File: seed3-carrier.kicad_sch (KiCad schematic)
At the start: 1 part

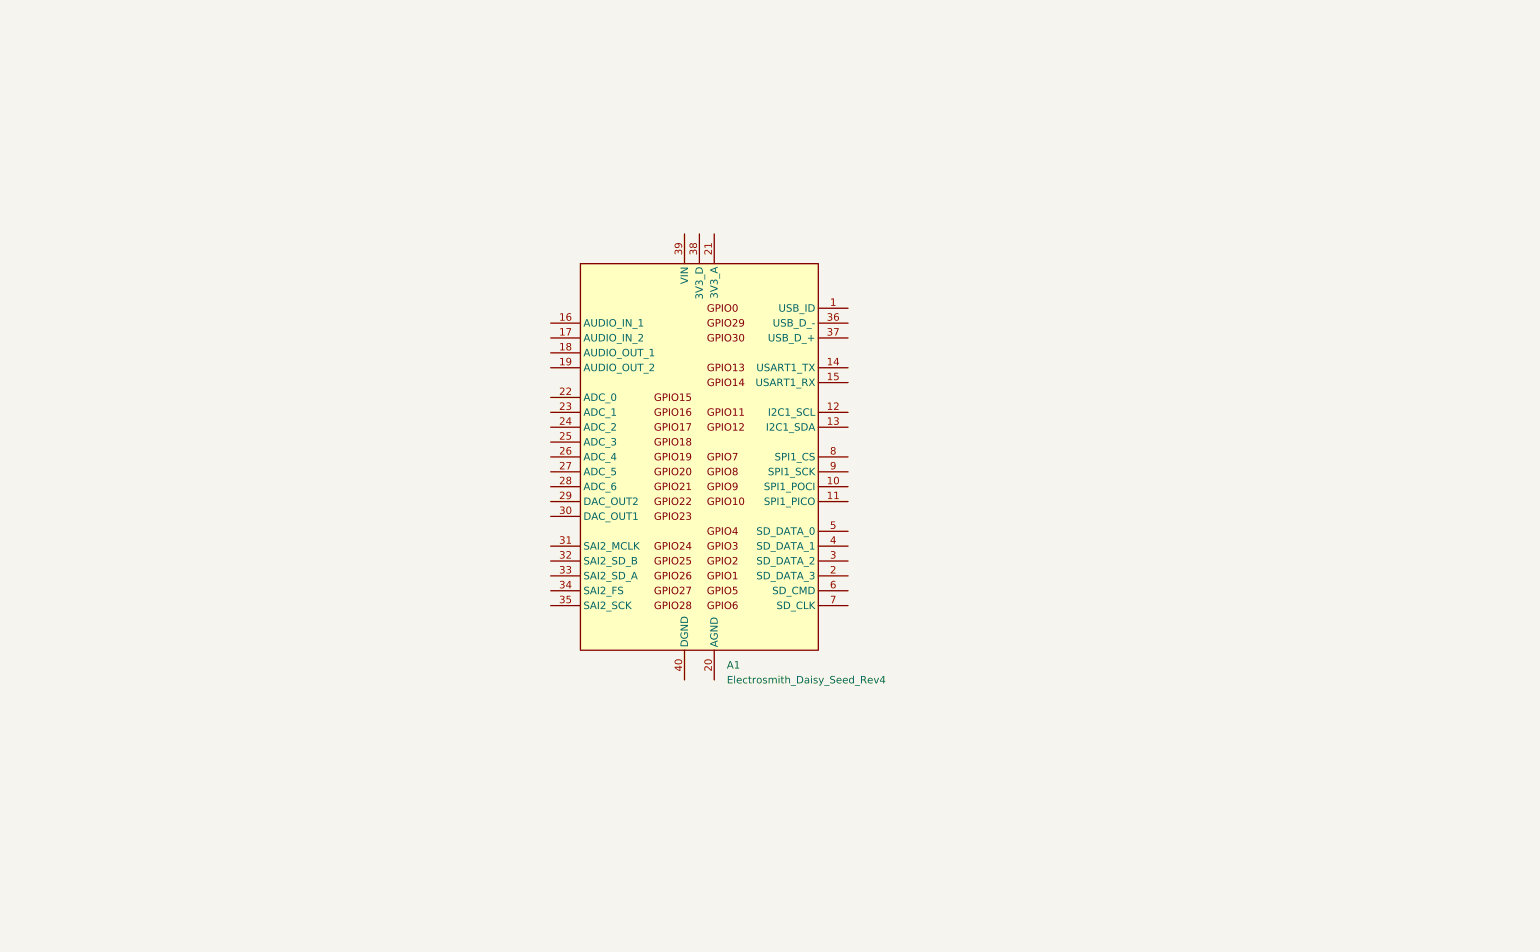
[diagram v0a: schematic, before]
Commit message: Complete carrier schematic with audio buffers, power, and display UART
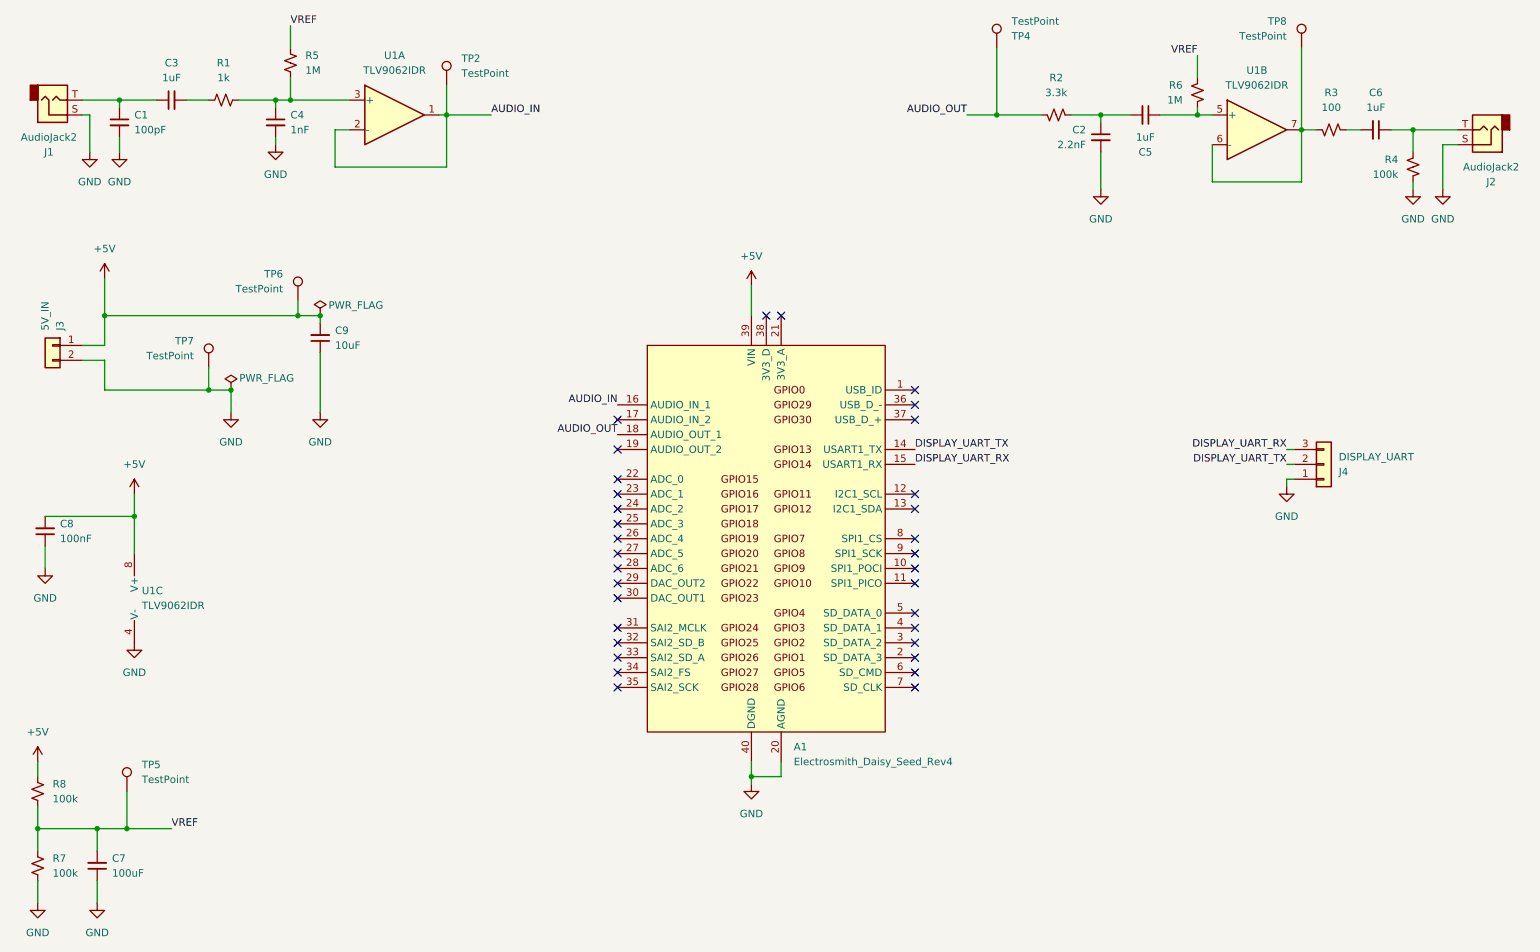
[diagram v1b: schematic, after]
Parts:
- added C1: 100pF, symbol Device:C_Small
- added C2: 2.2nF, symbol Device:C_Small
- added C3, C5, C6: 1uF, symbol Device:C_Small
- added C4: 1nF, symbol Device:C_Small
- added C7: 100uF, symbol Device:C_Small
- added C8: 100nF, symbol Device:C_Small
- added C9: 10uF, symbol Device:C_Small
- added J1, J2: AudioJack2, symbol Connector_Audio:AudioJack2
- added J3: 5V_IN, symbol Connector_Generic:Conn_01x02
- added J4: DISPLAY_UART, symbol Connector_Generic:Conn_01x03
- added R1: 1k, symbol Device:R_Small_US
- added R2: 3.3k, symbol Device:R_Small_US
- added R3: 100, symbol Device:R_Small_US
- added R4, R7, R8: 100k, symbol Device:R_Small_US
- added R5, R6: 1M, symbol Device:R_Small_US
- added TP2, TP4, TP5, TP6, TP7, TP8: TestPoint, symbol Connector:TestPoint
- added U1: TLV9062IDR, Package_SO:JEITA_SOIC-8_3.9x4.9mm_P1.27mm, symbol Amplifier_Operational:TL072
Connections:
- net DISPLAY_UART_TX: now reaches A1.14 (USART1_TX)
- net DISPLAY_UART_TX: now also J4.2 (Pin_2)
- net DISPLAY_UART_RX: now reaches A1.15 (USART1_RX)
- net DISPLAY_UART_RX: now also J4.3 (Pin_3)
- net AUDIO_IN: now reaches A1.16 (AUDIO_IN_1)
- net AUDIO_IN: now also TP2.1, U1.1, U1.2 (-)
- net AUDIO_OUT: now reaches A1.18 (AUDIO_OUT_1)
- net AUDIO_OUT: now also R2.2, TP4.1
- net GND: now reaches A1.20 (AGND)
- net GND: now also A1.40 (DGND), C1.2, C2.2, C4.2, C7.1, C8.1, C9.1, J1.S, J2.S, J3.2 (Pin_2), J4.1 (Pin_1), R4.1, R7.2, TP7.1, U1.4 (V-)
- net +5V: now reaches A1.39 (VIN)
- net +5V: now also C8.2, C9.2, J3.1 (Pin_1), R8.1, TP6.1, U1.8 (V+)
- new net: C1.1, C3.1, J1.T
- new net: C4.1, R1.2, R5.2, U1.3 (+)
- new net: C5.1, R6.2, U1.5 (+)
- new net: C2.1, C5.2, R2.1
- new net: C6.1, J2.T, R4.2
- new net: C3.2, R1.1
- new net: C6.2, R3.1
- new net: R3.2, TP8.1, U1.6 (-), U1.7
- new net VREF: C7.2, R5.1, R6.1, R7.1, R8.2, TP5.1
- no-connect marks 0 -> 33
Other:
- moved on the sheet: A1

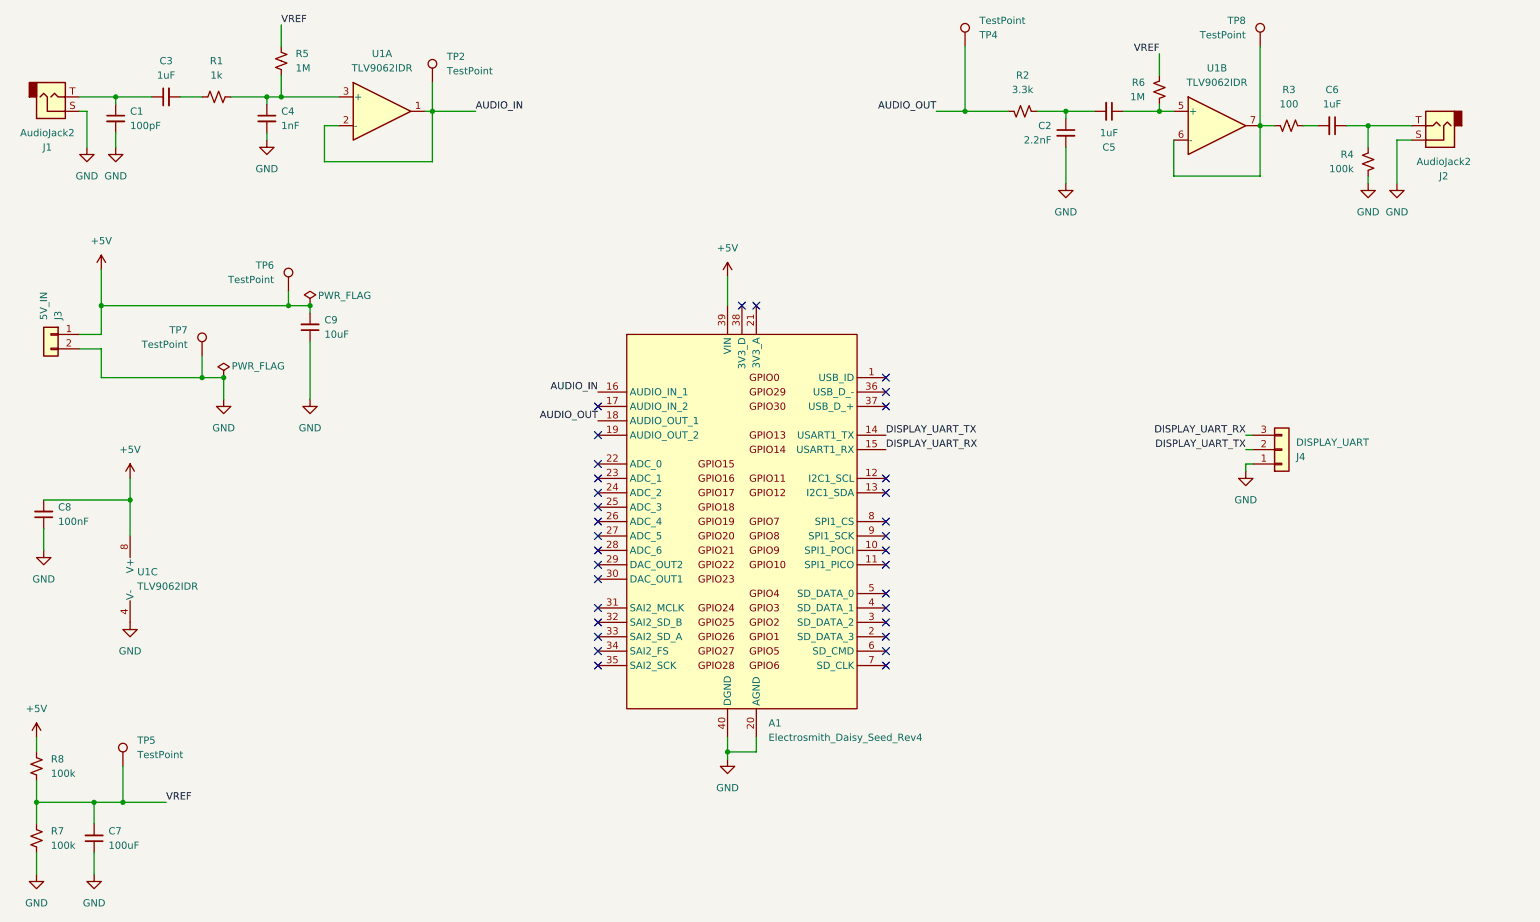
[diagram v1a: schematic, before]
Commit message: Refine audio filtering and bias values and add filtered pot controls
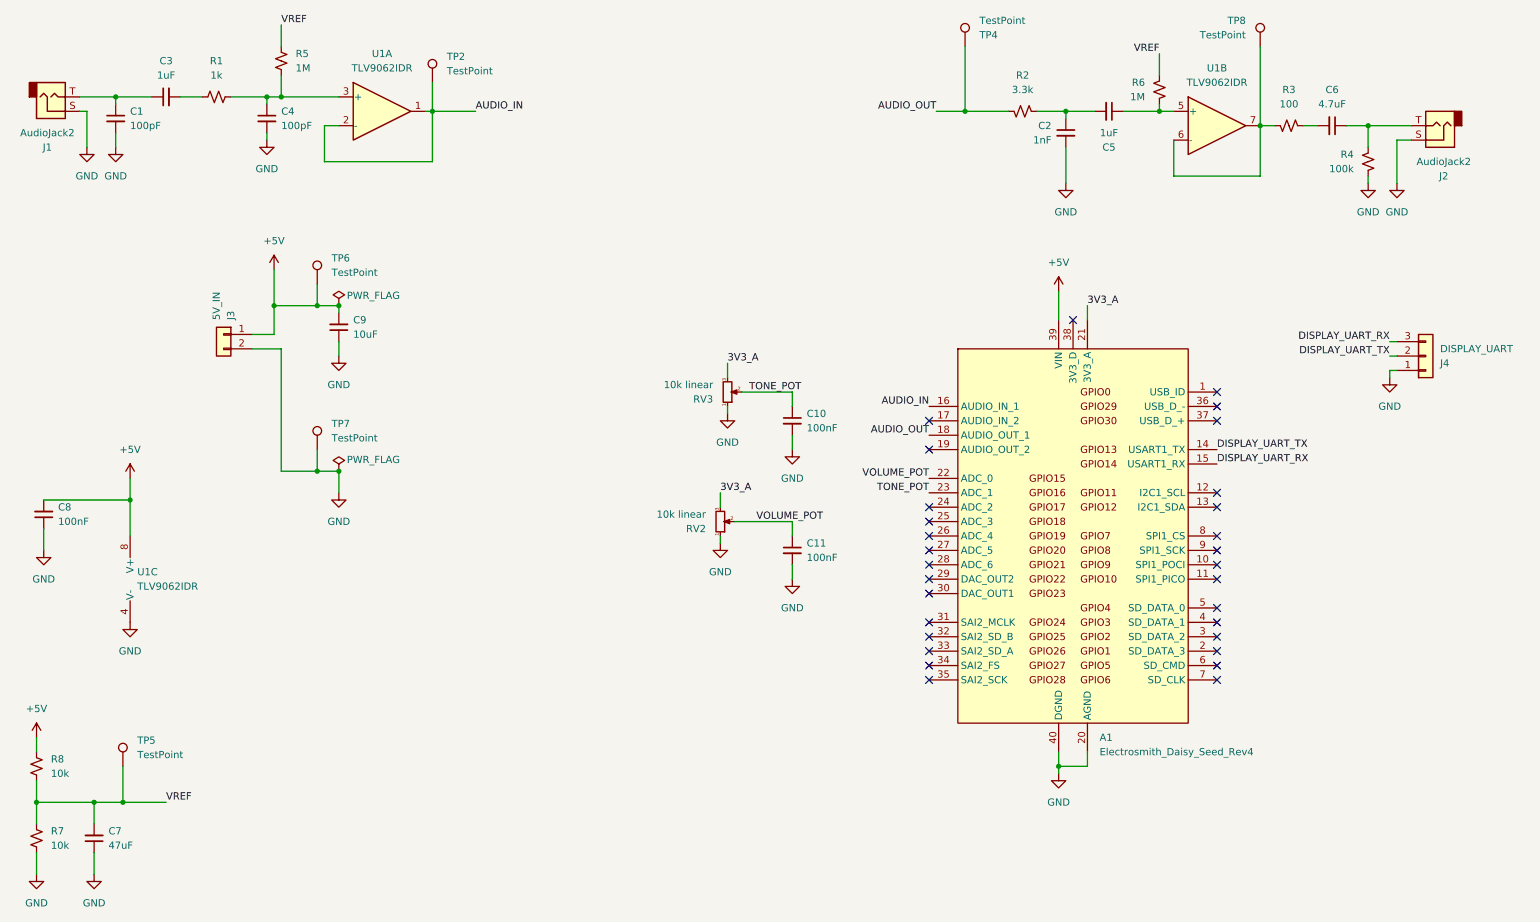
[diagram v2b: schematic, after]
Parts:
- added C10, C11: 100nF, symbol Device:C_Small
- added RV2, RV3: 10k linear, symbol Device:R_Potentiometer_Small
- C2: value 2.2nF -> 1nF
- C4: value 1nF -> 100pF
- C6: value 1uF -> 4.7uF
- C7: value 100uF -> 47uF
- R7, R8: value 100k -> 10k
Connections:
- net GND: now also C10.2, C11.2, RV2.1, RV3.1
- net 3V3_A: now reaches A1.21 (3V3_A)
- net 3V3_A: now also RV2.3, RV3.3
- net VOLUME_POT: now reaches A1.22 (ADC_0)
- net VOLUME_POT: now also C11.1, RV2.2
- net TONE_POT: now reaches A1.23 (ADC_1)
- net TONE_POT: now also C10.1, RV3.2
- no-connect marks 33 -> 30
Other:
- moved on the sheet: A1, C9, J3, J4, TP6, TP7

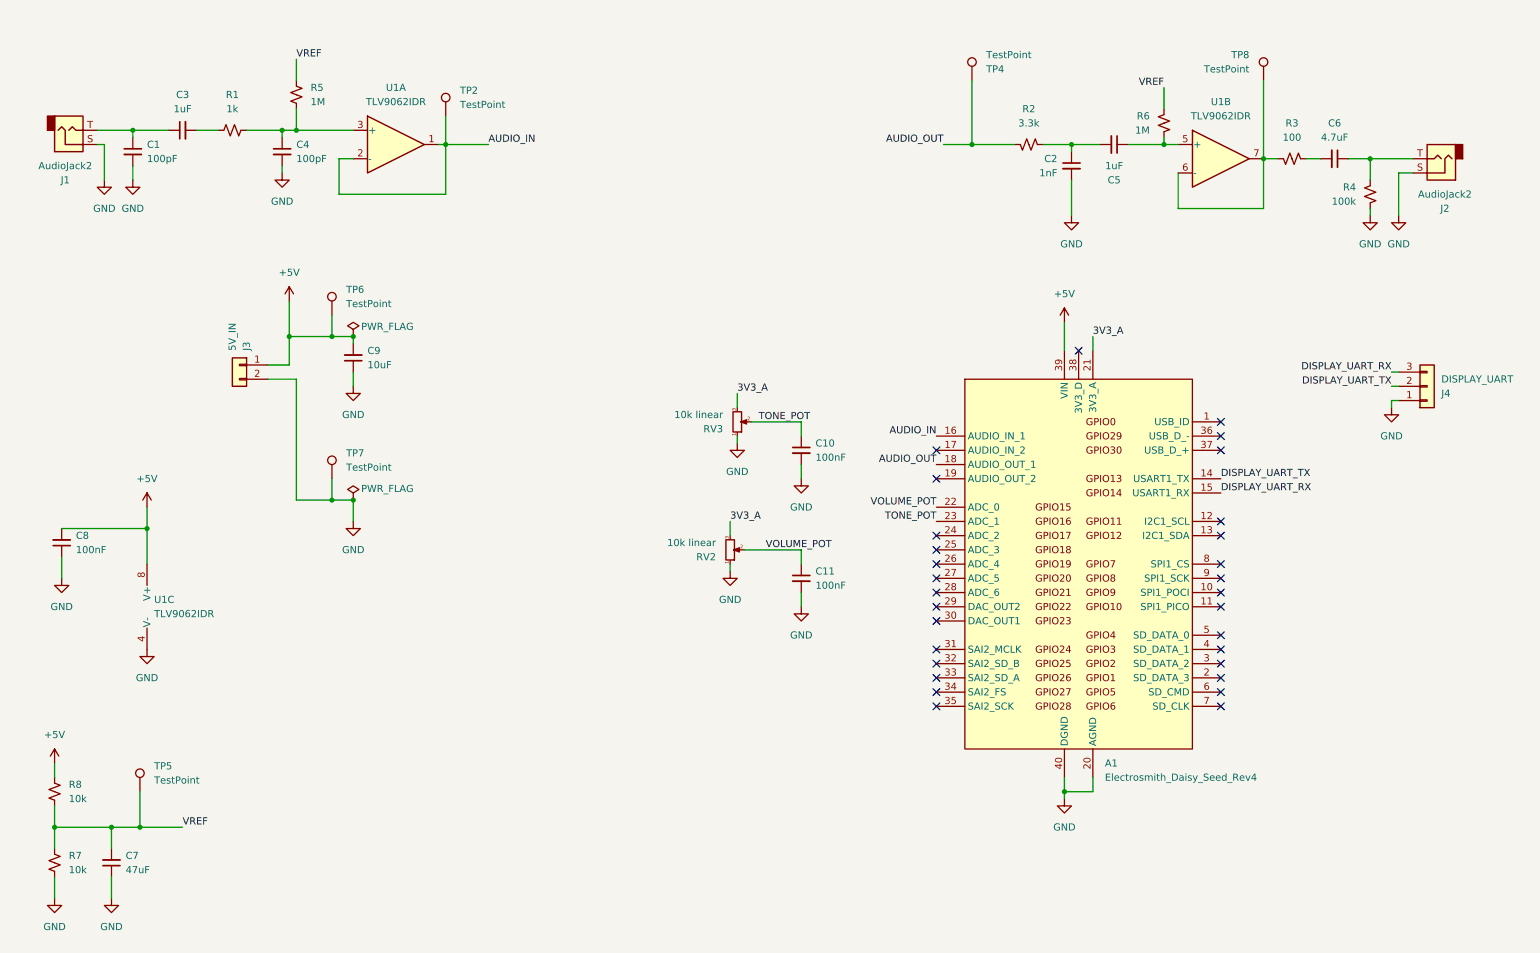
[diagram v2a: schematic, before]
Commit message: Organize schematic into readable functional sections
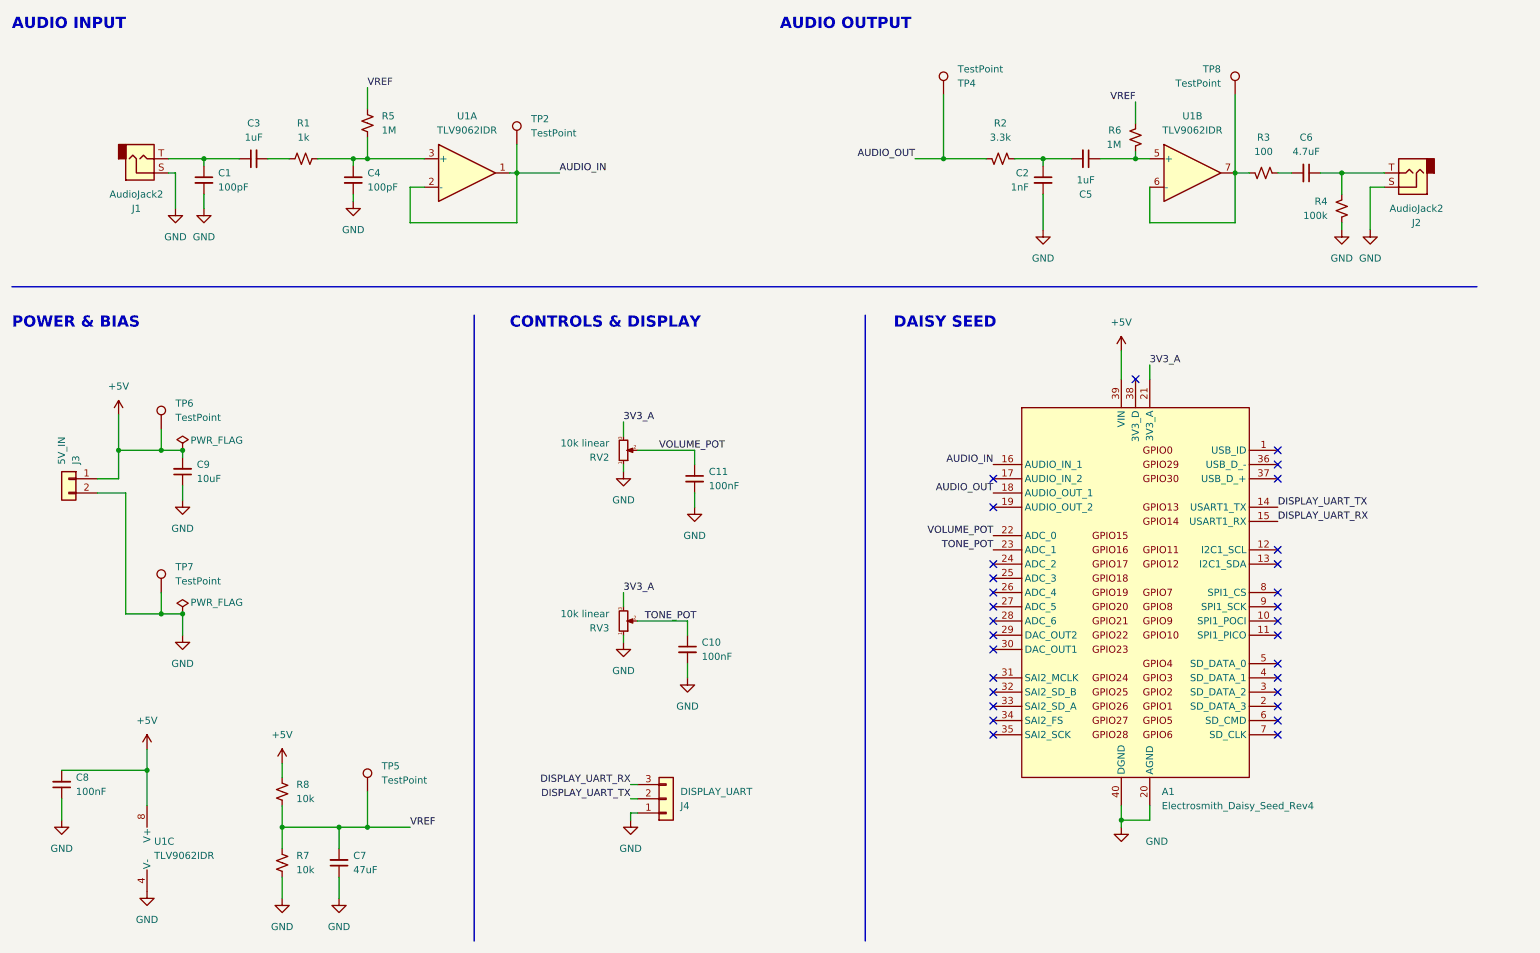
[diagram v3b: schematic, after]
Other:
- note added: "AUDIO INPUT"
- note added: "AUDIO OUTPUT"
- note added: "CONTROLS & DISPLAY"
- note added: "DAISY SEED"
- note added: "POWER & BIAS"
- title: (none) -> Seed3 Carrier
- moved on the sheet: A1, C1, C10, C11, C2, C3, C4, C5, C6, C7, C8, C9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
